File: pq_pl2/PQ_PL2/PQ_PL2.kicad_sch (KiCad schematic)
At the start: 81 parts, among them J1 BBL-110-Y-X, J2 BBL-110-Y-X, J3 BBL-110-Y-X, J4 BBL-110-Y-X, J5 U.FL-R-SMT, J6 MS-156C3, J7 MS-156C3, J8 U.FL-R-SMT, U1 LEE2-6+, U2 MAX2121, U3 LT5537, U4 LT3048, U5 TL071, Y1 ECS-TXO-2016MV

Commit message: Corrected the U.FL connector footprints on the PL2 Board. Added OBC&COMMS Bom
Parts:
- Annotation1: footprint -nsl_symbols:Bridgemaker -> symbols-nsl:Bridgemaker
- Annotation2: footprint -nsl_symbols:GRSS -> symbols-nsl:GRSS
- Annotation3: footprint -nsl_symbols:NSL_long -> symbols-nsl:NSL_long
- Annotation4: footprint -nsl_symbols:IEEE_logo -> symbols-nsl:IEEE_logo
- Annotation5: footprint -nsl_symbols:UPC_positiu -> symbols-nsl:UPC_positiu
- D1: footprint -nsl_passive:SLCD-61N8 -> passive-nsl:SLCD-61N8
- FL1: footprint -nsl_rf:GE0805C-3 -> rf-nsl:GE0805C-3
- J1, J2, J3, J4: footprint -nsl_connector:BBL-110-Y-X -> connector-nsl:BBL-110-Y-X
- J5, J8: footprint -nsl_connector:C.FL-R-SMT-1(90) -> connector-nsl:U.FL-R-SMT-1(10); symbol -nsl_connector:connector-coax -> connector-nsl:U.FL-R-SMT-1(10)
- J6, J7: footprint -nsl_connector:CoaxialSwitch_Hirose_MS-156C3_Horizontal -> connector-nsl:CoaxialSwitch_Hirose_MS-156C3_Horizontal
- U2: footprint -nsl_rf:QFN50P500X500X80-29N -> rf-nsl:QFN50P500X500X80-29N
- U3: footprint -nsl_rf:SON50P200X300X80-9N-D -> rf-nsl:SON50P200X300X80-9N-D
- U4: footprint -nsl_power:SON45P200X200X80-9N -> power-nsl:SON45P200X200X80-9N
- Y1: footprint -nsl_passive:ECSTXO201633320TR -> passive-nsl:ECSTXO201633320TR
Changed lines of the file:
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@@
       (effects (font (size 1.27 1.27)) (justify left bottom))
     )
-    (property "Footprint" "-nsl_connector:BBL-110-Y-X" (at 161.29 172.72 0)
+    (property "Footprint" "connector-nsl:BBL-110-Y-X" (at 161.29 172.72 0)
       (effects (font (size 1.27 1.27)) hide)
     )
@@
       (effects (font (size 1.27 1.27)) (justify left bottom))
     )
-    (property "Footprint" "-nsl_connector:BBL-110-Y-X" (at 224.79 172.72 0)
+    (property "Footprint" "connector-nsl:BBL-110-Y-X" (at 224.79 172.72 0)
       (effects (font (size 1.27 1.27)) hide)
     )
@@
       (effects (font (size 1.27 1.27)))
     )
-    (property "Footprint" "-nsl_rf:GE0805C-3" (at 178.054 83.312 0)
+    (property "Footprint" "rf-nsl:GE0805C-3" (at 178.054 83.312 0)
       (effects (font (size 1.27 1.27)) hide)
     )
@@
       (effects (font (size 1.27 1.27)) (justify left))
     )
-    (property "Footprint" "-nsl_symbols:UPC_positiu" (at 243.84 232.41 0)
+    (property "Footprint" "symbols-nsl:UPC_positiu" (at 243.84 232.41 0)
       (effects (font (size 1.27 1.27)) hide)
     )
@@
       (effects (font (size 1.27 1.27)))
     )
-    (property "Footprint" "-nsl_rf:SON50P200X300X80-9N-D" (at 125.73 173.99 0)
+    (property "Footprint" "rf-nsl:SON50P200X300X80-9N-D" (at 125.73 173.99 0)
       (effects (font (size 1.27 1.27)) hide)
     )
@@
       (effects (font (size 1.27 1.27)))
     )
-    (property "Footprint" "-nsl_power:SON45P200X200X80-9N" (at 293.37 176.53 0)
+    (property "Footprint" "power-nsl:SON45P200X200X80-9N" (at 293.37 176.53 0)
       (effects (font (size 1.27 1.27)) hide)
     )
@@
       (effects (font (size 1.27 1.27)) (justify left bottom))
     )
-    (property "Footprint" "-nsl_connector:CoaxialSwitch_Hirose_MS-156C3_Horizontal" (at 156.21 95.25 0)
+    (property "Footprint" "connector-nsl:CoaxialSwitch_Hirose_MS-156C3_Horizontal" (at 156.21 95.25 0)
       (effects (font (size 1.27 1.27)) hide)
     )
@@
       (effects (font (size 1.27 1.27)))
     )
-    (property "Footprint" "-nsl_passive:SLCD-61N8" (at 325.12 220.218 0)
+    (property "Footprint" "passive-nsl:SLCD-61N8" (at 325.12 220.218 0)
       (effects (font (size 1.27 1.27)) hide)
     )
@@
       (effects (font (size 1.27 1.27)) (justify left bottom))
     )
-    (property "Footprint" "-nsl_connector:BBL-110-Y-X" (at 254 172.72 0)
+    (property "Footprint" "connector-nsl:BBL-110-Y-X" (at 254 172.72 0)
       (effects (font (size 1.27 1.27)) hide)
     )
@@
     )
   )
-  (symbol (lib_id "-nsl_connector:connector-coax") (at 284.48 138.43 0) (mirror y) (unit 1)
+  (symbol (lib_id "connector-nsl:U.FL-R-SMT-1(10)") (at 284.48 138.43 0) (mirror y) (unit 1)
     (in_bom yes) (on_board yes) (dnp no)
     (property "Reference" "J8" (at 293.37 142.24 0)
@@
       (effects (font (size 1.27 1.27)) (justify left bottom))
     )
-    (property "Footprint" "-nsl_connector:C.FL-R-SMT-1(90)" (at 283.21 153.67 0)
+    (property "Footprint" "connector-nsl:U.FL-R-SMT-1(10)" (at 281.94 153.67 0)
       (effects (font (size 1.27 1.27)) hide)
     )
-    (property "Datasheet" "" (at 283.21 137.16 0)
+    (property "Datasheet" "" (at 284.48 138.43 0)
       (effects (font (size 1.27 1.27)) hide)
     )
@@
       (effects (font (size 1.27 1.27)))
     )
-    (property "Footprint" "-nsl_passive:ECSTXO201633320TR" (at 278.13 120.65 0)
+    (property "Footprint" "passive-nsl:ECSTXO201633320TR" (at 278.13 120.65 0)
       (effects (font (size 1.27 1.27)) hide)
     )
@@
       (effects (font (size 1.27 1.27)) (justify left bottom))
     )
-    (property "Footprint" "-nsl_connector:BBL-110-Y-X" (at 193.04 172.72 0)
+    (property "Footprint" "connector-nsl:BBL-110-Y-X" (at 193.04 172.72 0)
       (effects (font (size 1.27 1.27)) hide)
     )
@@
       (effects (font (size 1.27 1.27)) (justify left))
     )
-    (property "Footprint" "-nsl_symbols:GRSS" (at 123.19 232.41 0)
+    (property "Footprint" "symbols-nsl:GRSS" (at 123.19 232.41 0)
       (effects (font (size 1.27 1.27)) hide)
     )
@@
       (effects (font (size 1.27 1.27)) (justify left))
     )
-    (property "Footprint" "-nsl_symbols:IEEE_logo" (at 203.2 232.41 0)
+    (property "Footprint" "symbols-nsl:IEEE_logo" (at 203.2 232.41 0)
       (effects (font (size 1.27 1.27)) hide)
     )
@@
       (effects (font (size 1.27 1.27)))
     )
-    (property "Footprint" "-nsl_rf:QFN50P500X500X80-29N" (at 270.51 95.25 0)
+    (property "Footprint" "rf-nsl:QFN50P500X500X80-29N" (at 270.51 95.25 0)
       (effects (font (size 1.27 1.27)) hide)
     )
@@
       (effects (font (size 1.27 1.27)) (justify left))
     )
-    (property "Footprint" "-nsl_symbols:Bridgemaker" (at 86.36 232.41 0)
+    (property "Footprint" "symbols-nsl:Bridgemaker" (at 86.36 232.41 0)
       (effects (font (size 1.27 1.27)) hide)
     )
@@
       (effects (font (size 1.27 1.27)) (justify left))
     )
-    (property "Footprint" "-nsl_symbols:NSL_long" (at 162.56 232.41 0)
+    (property "Footprint" "symbols-nsl:NSL_long" (at 162.56 232.41 0)
       (effects (font (size 1.27 1.27)) hide)
     )
@@
       (effects (font (size 1.27 1.27)) (justify left bottom))
     )
-    (property "Footprint" "-nsl_connector:CoaxialSwitch_Hirose_MS-156C3_Horizontal" (at 231.14 88.9 0)
+    (property "Footprint" "connector-nsl:CoaxialSwitch_Hirose_MS-156C3_Horizontal" (at 231.14 88.9 0)
       (effects (font (size 1.27 1.27)) hide)
     )
@@
     )
   )
-  (symbol (lib_id "-nsl_connector:connector-coax") (at 88.9 88.9 0) (unit 1)
+  (symbol (lib_id "connector-nsl:U.FL-R-SMT-1(10)") (at 88.9 88.9 0) (unit 1)
     (in_bom yes) (on_board yes) (dnp no)
     (property "Reference" "J5" (at 87.63 84.455 0)
@@
       (effects (font (size 1.27 1.27)) (justify left bottom))
     )
-    (property "Footprint" "-nsl_connector:C.FL-R-SMT-1(90)" (at 90.17 104.14 0)
+    (property "Footprint" "connector-nsl:U.FL-R-SMT-1(10)" (at 91.44 104.14 0)
       (effects (font (size 1.27 1.27)) hide)
     )
-    (property "Datasheet" "" (at 90.17 87.63 0)
+    (property "Datasheet" "" (at 88.9 88.9 0)
       (effects (font (size 1.27 1.27)) hide)
     )

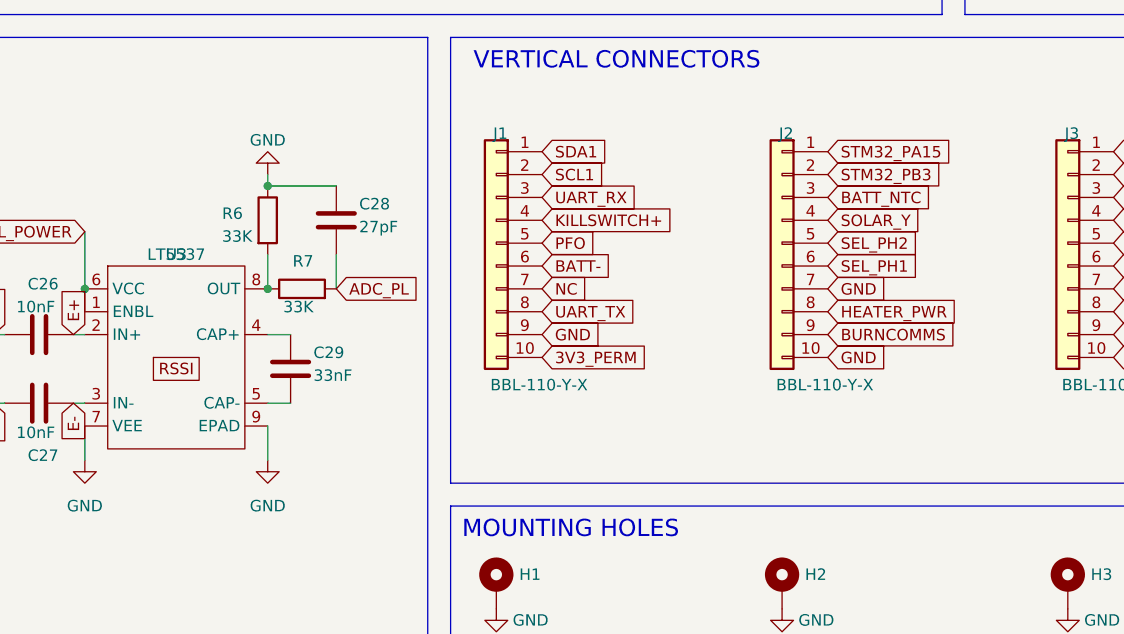
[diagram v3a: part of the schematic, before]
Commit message: J2(2) pin rename to SWO; DRC
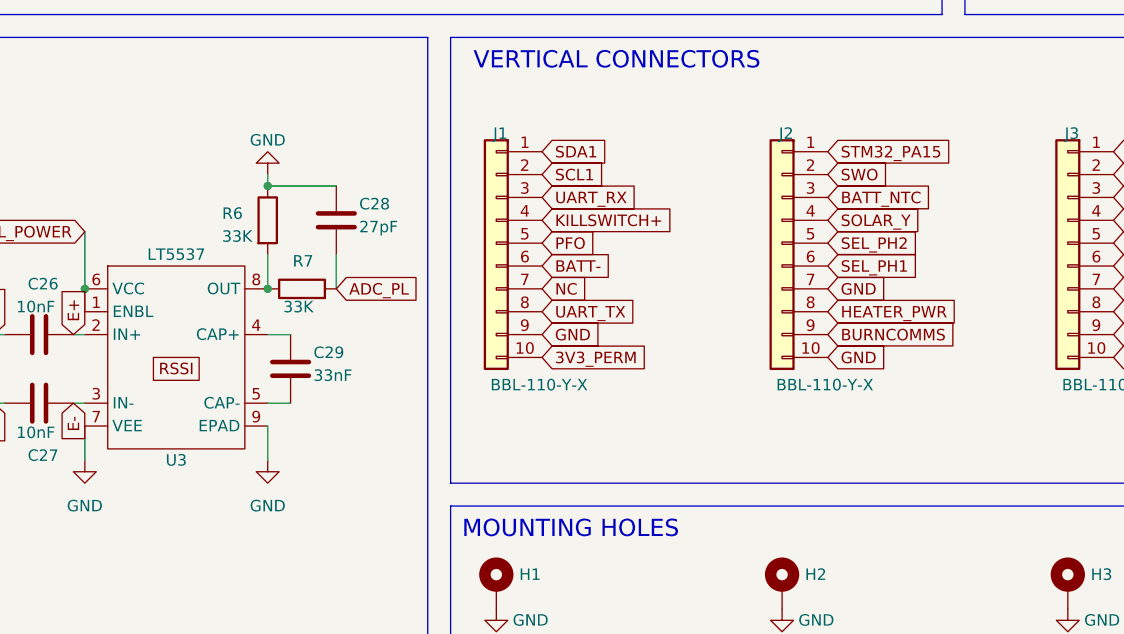
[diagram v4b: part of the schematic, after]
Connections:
- net STM32_PB3 renamed SWO
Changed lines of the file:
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@@
     )
   )
-  (global_label "STM32_PB3" (shape input) (at 198.12 165.1 0) (fields_autoplaced)
-    (effects (font (size 1.27 1.27)) (justify left))
-    (property "Intersheetrefs" "${INTERSHEET_REFS}" (at 211.2979 165.0206 0)
+  (global_label "SWO" (shape input) (at 198.12 165.1 0) (fields_autoplaced)
+    (effects (font (size 1.27 1.27)) (justify left))
+    (property "Intersheetrefs" "${INTERSHEET_REFS}" (at 205.0966 165.1 0)
       (effects (font (size 1.27 1.27)) (justify left) hide)
     )
@@
   )
   (symbol (lib_id "-nsl_rf:LT5537") (at 125.73 186.69 0) (unit 1)
-    (in_bom yes) (on_board yes) (dnp no) (fields_autoplaced)
-    (property "Reference" "U3" (at 125.73 173.99 0)
+    (in_bom yes) (on_board yes) (dnp no)
+    (property "Reference" "U3" (at 125.73 196.85 0)
       (effects (font (size 1.27 1.27)))
     )

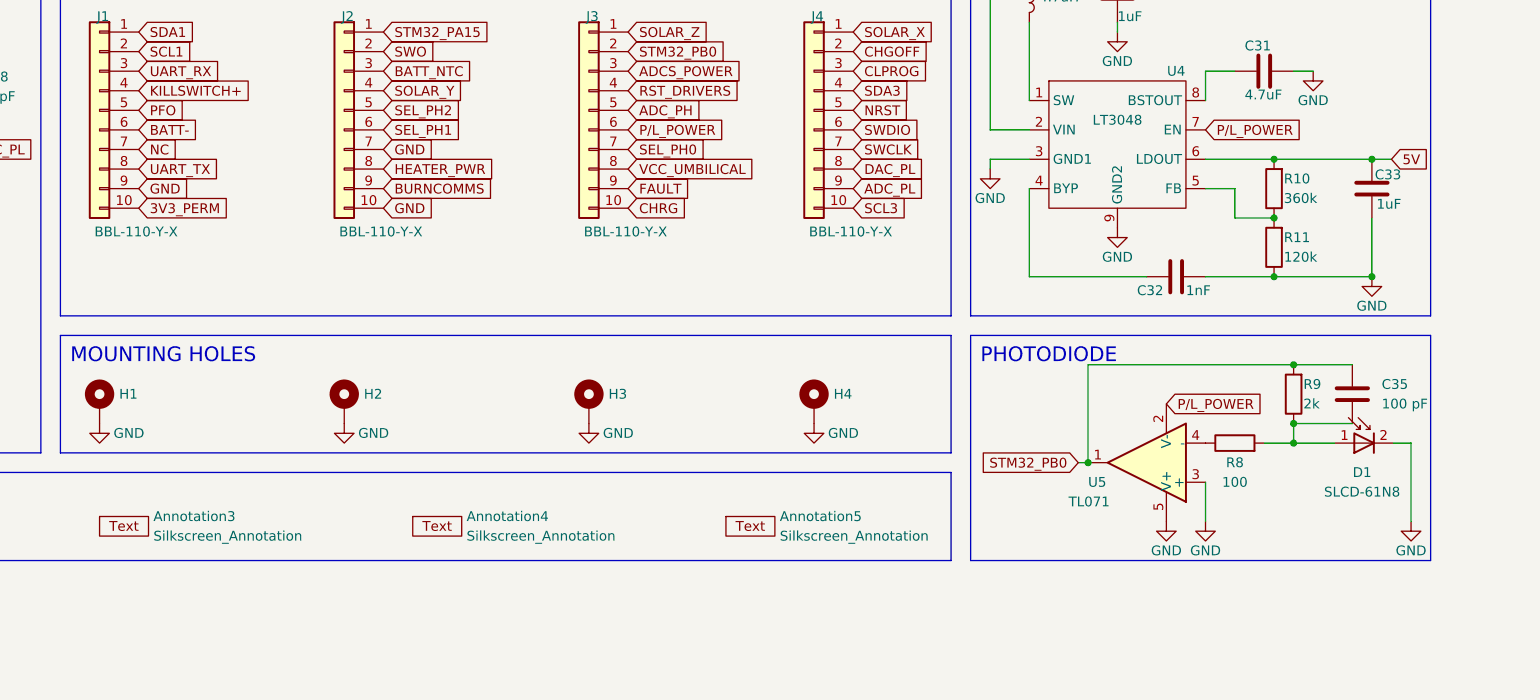
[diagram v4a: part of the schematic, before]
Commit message: PL2 Modifications added
Phtodiode ampllifier deleted
Pins restructured
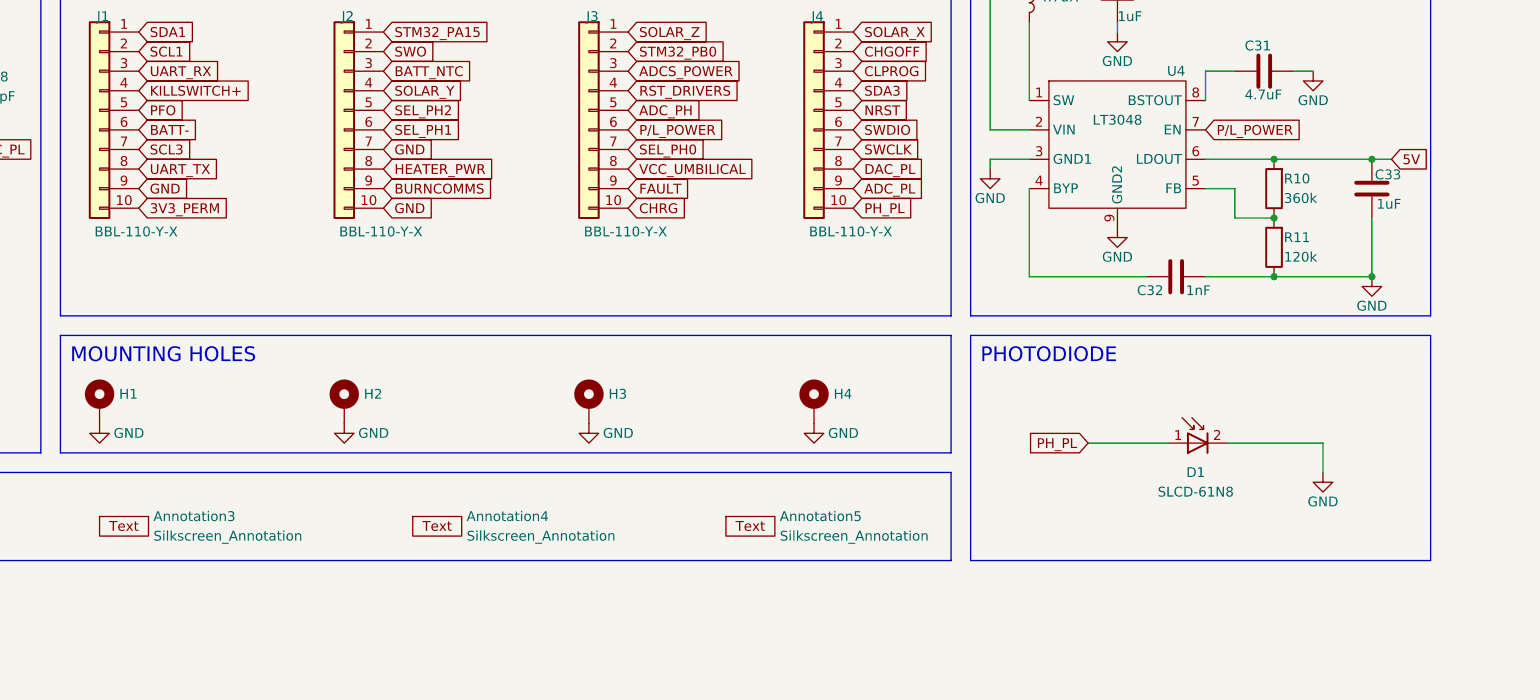
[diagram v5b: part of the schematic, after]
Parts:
- removed C35: 100 pF, Capacitor_SMD:C_0603_1608Metric, symbol Device:C
- removed R8: 100, Resistor_SMD:R_0603_1608Metric, symbol Device:R
- removed R9: 2k, Resistor_SMD:R_0603_1608Metric, symbol Device:R
- removed U5: TL071, Package_TO_SOT_SMD:TSOT-23-5, symbol Amplifier_Operational:AD8603
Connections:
- net NC is gone; now on net SCL3: J1.7 (Pin_7)
- net SCL3: no longer J4.10 (Pin_10)
- net PH_PL: now reaches D1.1
- net PH_PL: now also J4.10 (Pin_10)
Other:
- moved on the sheet: D1
